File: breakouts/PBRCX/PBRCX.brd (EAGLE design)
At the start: 13.6 x 17.9 mm, 6 parts

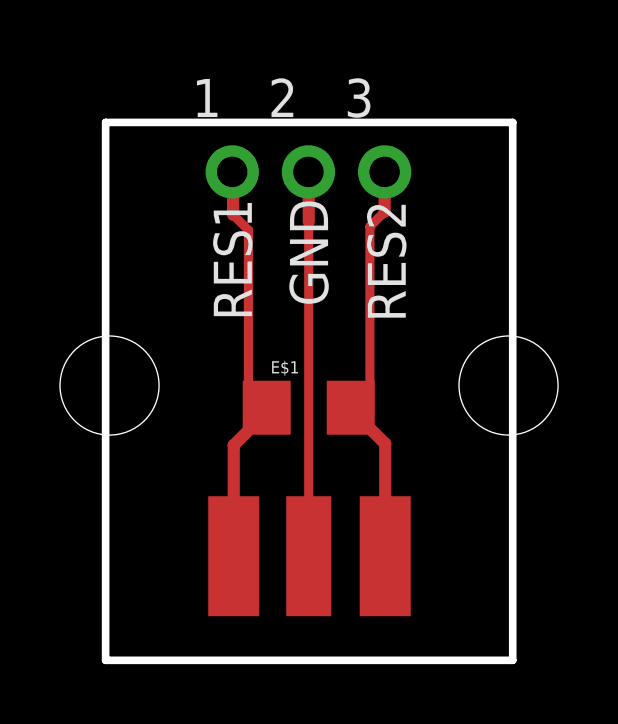
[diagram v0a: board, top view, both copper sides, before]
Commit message: PBRCX - moved ground to outside pin.
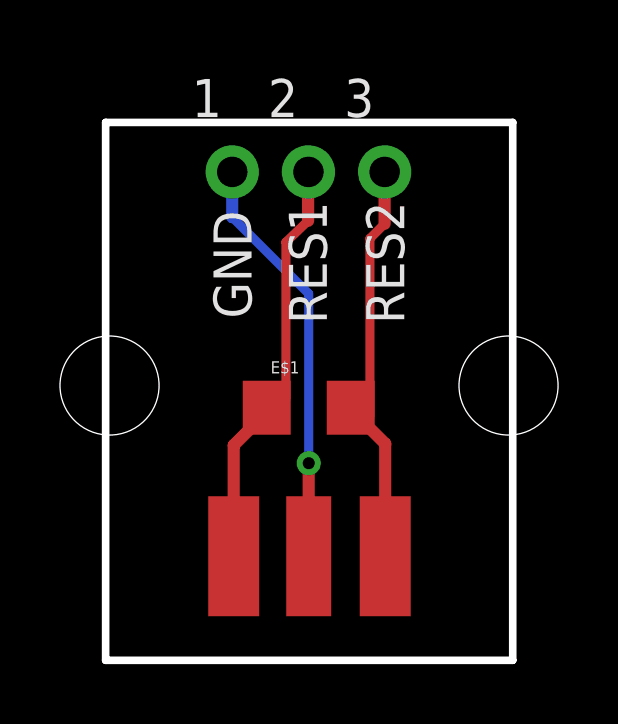
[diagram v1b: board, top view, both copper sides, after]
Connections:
- removed net D-: 1.1
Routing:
- net S$3: track 0.00 -> 10.8 mm
- net S$4: track 11.1 -> 1.40 mm
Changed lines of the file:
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@@
 <wire x1="22.05" y1="23.06" x2="22.05" y2="5.13" width="0.254" layer="20"/>
 <wire x1="22.05" y1="5.13" x2="8.48" y2="5.13" width="0.254" layer="20"/>
-<text x="14.625" y="20.52" size="1.27" layer="121" font="vector" ratio="15" rot="R270">GND</text>
-<text x="12.085" y="20.52" size="1.27" layer="121" font="vector" ratio="15" rot="R270">RES1</text>
-<text x="17.215" y="20.47" size="1.27" layer="121" font="vector" ratio="15" rot="R270">RES2</text>
+<text x="12.075" y="20.12" size="1.27" layer="121" font="vector" ratio="15" rot="R270">GND</text>
+<text x="14.585" y="20.42" size="1.27" layer="121" font="vector" ratio="15" rot="R270">RES1</text>
+<text x="17.165" y="20.42" size="1.27" layer="121" font="vector" ratio="15" rot="R270">RES2</text>
 <text x="19.93" y="18.03" size="1.27" layer="122" font="vector" rot="MR0">quilix.com</text>
 <rectangle x1="16.95" y1="6.6" x2="18.65" y2="10.6" layer="1"/>
@@
 <signals>
 <signal name="D-">
-<contactref element="1" pad="1"/>
-<wire x1="12.7" y1="21.41" x2="12.73" y2="21.38" width="0.4064" layer="1"/>
-<wire x1="12.73" y1="21.38" x2="12.73" y2="19.98" width="0.4064" layer="1"/>
-<wire x1="12.73" y1="19.98" x2="13.24" y2="19.47" width="0.3048" layer="1"/>
-<wire x1="13.24" y1="19.47" x2="13.24" y2="13.65" width="0.3048" layer="1"/>
+<wire x1="15.23" y1="21.38" x2="15.23" y2="19.78" width="0.4064" layer="1"/>
+<wire x1="15.23" y1="19.78" x2="14.49" y2="19.07" width="0.3048" layer="1"/>
+<wire x1="14.49" y1="19.07" x2="14.49" y2="13.85" width="0.3048" layer="1"/>
 </signal>
 <signal name="S$1">
 <contactref element="3" pad="1"/>
-<wire x1="17.78" y1="21.41" x2="17.78" y2="20.08" width="0.4064" layer="1"/>
-<wire x1="17.78" y1="20.08" x2="17.29" y2="19.59" width="0.3048" layer="1"/>
-<wire x1="17.29" y1="19.59" x2="17.29" y2="13.25" width="0.3048" layer="1"/>
+<wire x1="17.78" y1="21.41" x2="17.78" y2="19.68" width="0.4064" layer="1"/>
+<wire x1="17.78" y1="19.68" x2="17.29" y2="19.19" width="0.3048" layer="1"/>
+<wire x1="17.29" y1="19.19" x2="17.29" y2="13.25" width="0.3048" layer="1"/>
 </signal>
 <signal name="S$4">
-<wire x1="15.25" y1="10.3" x2="15.25" y2="19.75" width="0.3048" layer="1"/>
-<wire x1="15.25" y1="19.75" x2="15.25" y2="21.4" width="0.4064" layer="1"/>
+<wire x1="15.25" y1="10.3" x2="15.25" y2="10.35" width="0.3048" layer="1"/>
+<wire x1="15.25" y1="10.35" x2="15.25" y2="11.7" width="0.4064" layer="1"/>
 </signal>
 <signal name="S$5">
@@
 <wire x1="17.8" y1="12.35" x2="17.8" y2="10.15" width="0.4064" layer="1"/>
 </signal>
+<signal name="S$2">
+<via x="15.25" y="11.7" extent="1-16" drill="0.4"/>
+</signal>
+<signal name="S$3">
+<wire x1="12.7" y1="21.4" x2="12.7" y2="19.9" width="0.4064" layer="16"/>
+<wire x1="12.7" y1="19.9" x2="15.25" y2="17.35" width="0.3048" layer="16"/>
+<wire x1="15.25" y1="17.35" x2="15.25" y2="11.65" width="0.3048" layer="16"/>
+</signal>
 </signals>
